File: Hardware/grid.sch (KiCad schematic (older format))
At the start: 269 parts, among them Q1 BSS83P, Q10 BSS83P, Q11 BSS83P, Q12 BSS83P, Q13 BSS83P, Q14 BSS83P, Q15 BSS83P, Q16 BSS83P, Q17 BSS83P, Q18 BSS83P, Q19 BSS83P, Q2 BSS83P, Q20 BSS83P, Q21 NX7002AK, Q22 NX7002AK, Q23 NX7002AK, Q24 NX7002AK, Q25 NX7002AK, Q26 NX7002AK, Q27 NX7002AK, Q28 NX7002AK, Q29 NX7002AK, Q3 BSS83P, Q30 NX7002AK, Q31 NX7002AK, Q32 NX7002AK, Q4 BSS83P, Q5 BSS83P, Q6 BSS83P, Q7 BSS83P, Q8 BSS83P, Q9 BSS83P, SW1 Button_matrix_4x4, SW10 SW_Push, SW11 SW_Push, SW12 SW_Push, SW13 SW_Push, SW14 SW_Push, SW15 SW_Push, SW16 SW_Push, SW17 SW_Push, SW18 SW_Push, SW19 SW_Push, SW2 Button_matrix_4x4, SW20 SW_Push, SW3 Button_matrix_4x4, SW4 Button_matrix_4x4, SW5 SW_Push, SW6 SW_Push, SW7 SW_Push, SW8 SW_Push, SW9 SW_Push, U2 74HC138, U3 74HC138, U4 74HC138

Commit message: linked footprints with 3D models in project directory
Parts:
- R21, R22, R23, R24: value 10K -> 1K
- R25, R26, R27, R28, R33, R34, R35, R36, R41, R42, R43, R44: value 100 -> 100R
- U2, U3, U4: Catalog link (none) -> http://uk.farnell.com/texas-instruments/sn74hc138pw/ic-deco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
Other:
- moved on the sheet: Q21, Q22, Q23, Q24, Q25, Q26, Q27, Q28, Q29, Q30, Q31, Q32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

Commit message: added BOM, changed names of some components in the schematic
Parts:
- Q1, Q10, Q11, Q12, Q13, Q14, Q15, Q16, Q17, Q18, Q19, Q2, Q20, Q3, Q4, Q5, Q6, Q7, Q8, Q9: value BSS83P -> BSH205G2
- U2, U3, U4: value 74HC138 -> SN74HC138PW
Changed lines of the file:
@@
 P 8200 2750
 F 0 "Q2" H 7900 2900 50  0000 L CNN
-F 1 "BSS83P" H 7900 3000 50  0000 L CNN
+F 1 "BSH205G2" H 7900 3000 50  0000 L CNN
 F 2 "project_library:SOT-23" H 8400 2675 50  0001 L CIN
 F 3 "" H 8200 2750 50  0001 L CNN
@@
 P 7650 2750
 F 0 "Q1" H 7350 2900 50  0000 L CNN
-F 1 "BSS83P" H 7350 3000 50  0000 L CNN
+F 1 "BSH205G2" H 7350 3000 50  0000 L CNN
 F 2 "project_library:SOT-23" H 7850 2675 50  0001 L CIN
 F 3 "" H 7650 2750 50  0001 L CNN
@@
 P 9450 2750
 F 0 "Q4" H 9150 2900 50  0000 L CNN
-F 1 "BSS83P" H 9150 3000 50  0000 L CNN
+F 1 "BSH205G2" H 9150 3000 50  0000 L CNN
 F 2 "project_library:SOT-23" H 9650 2675 50  0001 L CIN
 F 3 "" H 9450 2750 50  0001 L CNN
@@
 P 8900 2750
 F 0 "Q3" H 8600 2900 50  0000 L CNN
-F 1 "BSS83P" H 8600 3000 50  0000 L CNN
+F 1 "BSH205G2" H 8600 3000 50  0000 L CNN
 F 2 "project_library:SOT-23" H 9100 2675 50  0001 L CIN
 F 3 "" H 8900 2750 50  0001 L CNN
@@
 P 10700 2750
 F 0 "Q6" H 10400 2900 50  0000 L CNN
-F 1 "BSS83P" H 10400 3000 50  0000 L CNN
+F 1 "BSH205G2" H 10400 3000 50  0000 L CNN
 F 2 "project_library:SOT-23" H 10900 2675 50  0001 L CIN
 F 3 "" H 10700 2750 50  0001 L CNN
@@
 P 10150 2750
 F 0 "Q5" H 9850 2900 50  0000 L CNN
-F 1 "BSS83P" H 9850 3000 50  0000 L CNN
+F 1 "BSH205G2" H 9850 3000 50  0000 L CNN
 F 2 "project_library:SOT-23" H 10350 2675 50  0001 L CIN
 F 3 "" H 10150 2750 50  0001 L CNN
@@
 P 11950 2750
 F 0 "Q8" H 11650 2900 50  0000 L CNN
-F 1 "BSS83P" H 11650 3000 50  0000 L CNN
+F 1 "BSH205G2" H 11650 3000 50  0000 L CNN
 F 2 "project_library:SOT-23" H 12150 2675 50  0001 L CIN
 F 3 "" H 11950 2750 50  0001 L CNN
@@
 P 11400 2750
 F 0 "Q7" H 11100 2900 50  0000 L CNN
-F 1 "BSS83P" H 11100 3000 50  0000 L CNN
+F 1 "BSH205G2" H 11100 3000 50  0000 L CNN
 F 2 "project_library:SOT-23" H 11600 2675 50  0001 L CIN
 F 3 "" H 11400 2750 50  0001 L CNN
@@
 P 13200 2750
 F 0 "Q10" H 12900 2900 50  0000 L CNN
-F 1 "BSS83P" H 12900 3000 50  0000 L CNN
+F 1 "BSH205G2" H 12900 3000 50  0000 L CNN
 F 2 "project_library:SOT-23" H 13400 2675 50  0001 L CIN
 F 3 "" H 13200 2750 50  0001 L CNN
@@
 P 12650 2750
 F 0 "Q9" H 12350 2900 50  0000 L CNN
-F 1 "BSS83P" H 12350 3000 50  0000 L CNN
+F 1 "BSH205G2" H 12350 3000 50  0000 L CNN
 F 2 "project_library:SOT-23" H 12850 2675 50  0001 L CIN
 F 3 "" H 12650 2750 50  0001 L CNN
@@
 P 14450 2750
 F 0 "Q12" H 14150 2900 50  0000 L CNN
-F 1 "BSS83P" H 14150 3000 50  0000 L CNN
+F 1 "BSH205G2" H 14150 3000 50  0000 L CNN
 F 2 "project_library:SOT-23" H 14650 2675 50  0001 L CIN
 F 3 "" H 14450 2750 50  0001 L CNN
@@
 P 13900 2750
 F 0 "Q11" H 13600 2900 50  0000 L CNN
-F 1 "BSS83P" H 13600 3000 50  0000 L CNN
+F 1 "BSH205G2" H 13600 3000 50  0000 L CNN
 F 2 "project_library:SOT-23" H 14100 2675 50  0001 L CIN
 F 3 "" H 13900 2750 50  0001 L CNN
@@
 P 15700 2750
 F 0 "Q14" H 15400 2900 50  0000 L CNN
-F 1 "BSS83P" H 15400 3000 50  0000 L CNN
+F 1 "BSH205G2" H 15400 3000 50  0000 L CNN
 F 2 "project_library:SOT-23" H 15900 2675 50  0001 L CIN
 F 3 "" H 15700 2750 50  0001 L CNN
@@
 P 15150 2750
 F 0 "Q13" H 14850 2900 50  0000 L CNN
-F 1 "BSS83P" H 14850 3000 50  0000 L CNN
+F 1 "BSH205G2" H 14850 3000 50  0000 L CNN
 F 2 "project_library:SOT-23" H 15350 2675 50  0001 L CIN
 F 3 "" H 15150 2750 50  0001 L CNN
@@
 P 16950 2750
 F 0 "Q16" H 16650 2900 50  0000 L CNN
-F 1 "BSS83P" H 16650 3000 50  0000 L CNN
+F 1 "BSH205G2" H 16650 3000 50  0000 L CNN
 F 2 "project_library:SOT-23" H 17150 2675 50  0001 L CIN
 F 3 "" H 16950 2750 50  0001 L CNN
@@
 P 16400 2750
 F 0 "Q15" H 16100 2900 50  0000 L CNN
-F 1 "BSS83P" H 16100 3000 50  0000 L CNN
+F 1 "BSH205G2" H 16100 3000 50  0000 L CNN
 F 2 "project_library:SOT-23" H 16600 2675 50  0001 L CIN
 F 3 "" H 16400 2750 50  0001 L CNN
@@
 P 10250 13500
 F 0 "U4" H 10350 14000 50  0000 C CNN
-F 1 "74HC138" H 10550 13000 50  0000 C CNN
+F 1 "SN74HC138PW" H 10550 13000 50  0000 C CNN
 F 2 "project_library:TSSOP-16_4.4x5mm_Pitch0.65mm" H 10250 13500 50  0001 C CNN
 F 3 "" H 10250 13500 50  0001 C CNN
@@
 P 7700 13500
 F 0 "U3" H 7800 14000 50  0000 C CNN
-F 1 "74HC138" H 8000 13000 50  0000 C CNN
+F 1 "SN74HC138PW" H 8000 13000 50  0000 C CNN
 F 2 "project_library:TSSOP-16_4.4x5mm_Pitch0.65mm" H 7700 13500 50  0001 C CNN
 F 3 "" H 7700 13500 50  0001 C CNN
@@
 P 5150 13500
 F 0 "U2" H 5250 14000 50  0000 C CNN
-F 1 "74HC138" H 5450 13000 50  0000 C CNN
+F 1 "SN74HC138PW" H 5450 13000 50  0000 C CNN
 F 2 "project_library:TSSOP-16_4.4x5mm_Pitch0.65mm" H 5150 13500 50  0001 C CNN
 F 3 "" H 5150 13500 50  0001 C CNN
@@
 P 18700 2750
 F 0 "Q18" H 18400 2900 50  0000 L CNN
-F 1 "BSS83P" H 18400 3000 50  0000 L CNN
+F 1 "BSH205G2" H 18400 3000 50  0000 L CNN
 F 2 "project_library:SOT-23" H 18900 2675 50  0001 L CIN
 F 3 "" H 18700 2750 50  0001 L CNN
@@
 P 18150 2750
 F 0 "Q17" H 17850 2900 50  0000 L CNN
-F 1 "BSS83P" H 17850 3000 50  0000 L CNN
+F 1 "BSH205G2" H 17850 3000 50  0000 L CNN
 F 2 "project_library:SOT-23" H 18350 2675 50  0001 L CIN
 F 3 "" H 18150 2750 50  0001 L CNN
@@
 P 19950 2750
 F 0 "Q20" H 19650 2900 50  0000 L CNN
-F 1 "BSS83P" H 19650 3000 50  0000 L CNN
+F 1 "BSH205G2" H 19650 3000 50  0000 L CNN
 F 2 "project_library:SOT-23" H 20150 2675 50  0001 L CIN
 F 3 "" H 19950 2750 50  0001 L CNN
@@
 P 19400 2750
 F 0 "Q19" H 19100 2900 50  0000 L CNN
-F 1 "BSS83P" H 19100 3000 50  0000 L CNN
+F 1 "BSH205G2" H 19100 3000 50  0000 L CNN
 F 2 "project_library:SOT-23" H 19600 2675 50  0001 L CIN
 F 3 "" H 19400 2750 50  0001 L CNN

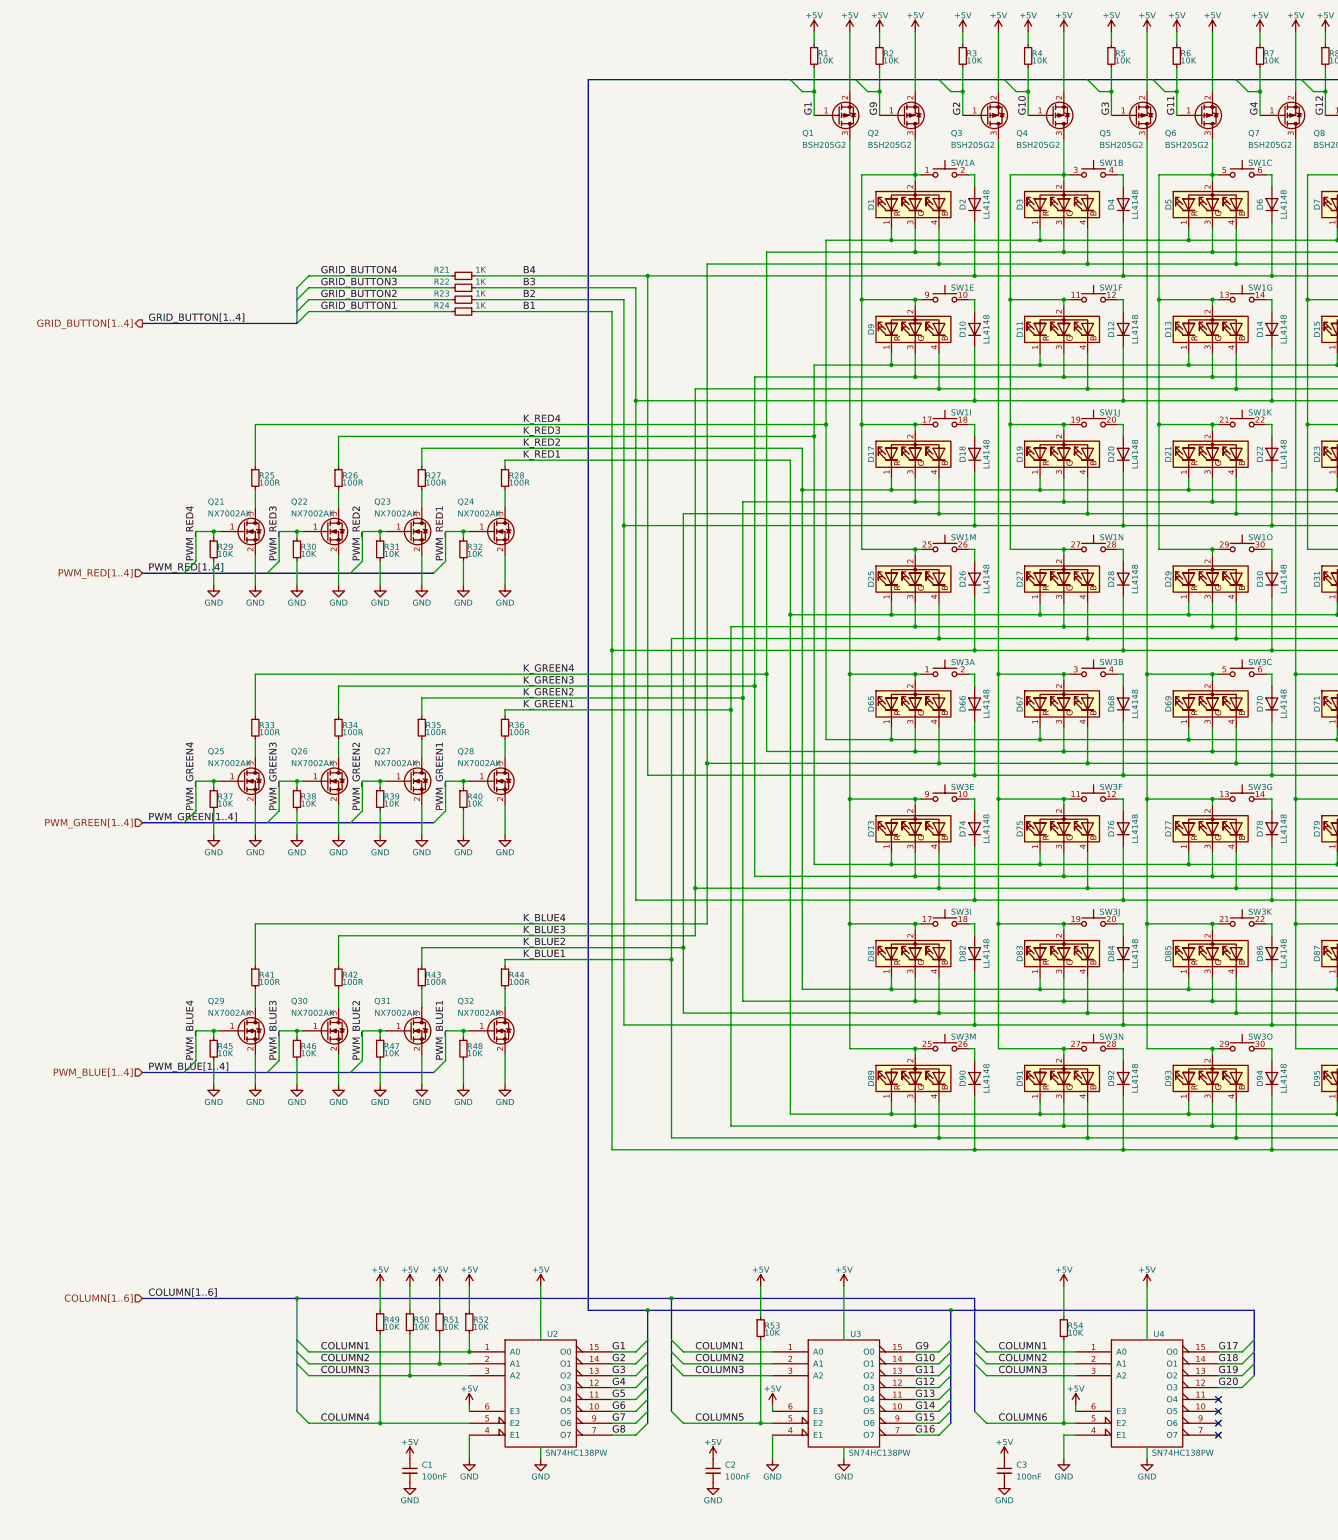
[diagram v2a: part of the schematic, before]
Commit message: copied project cache library to project_library.lib
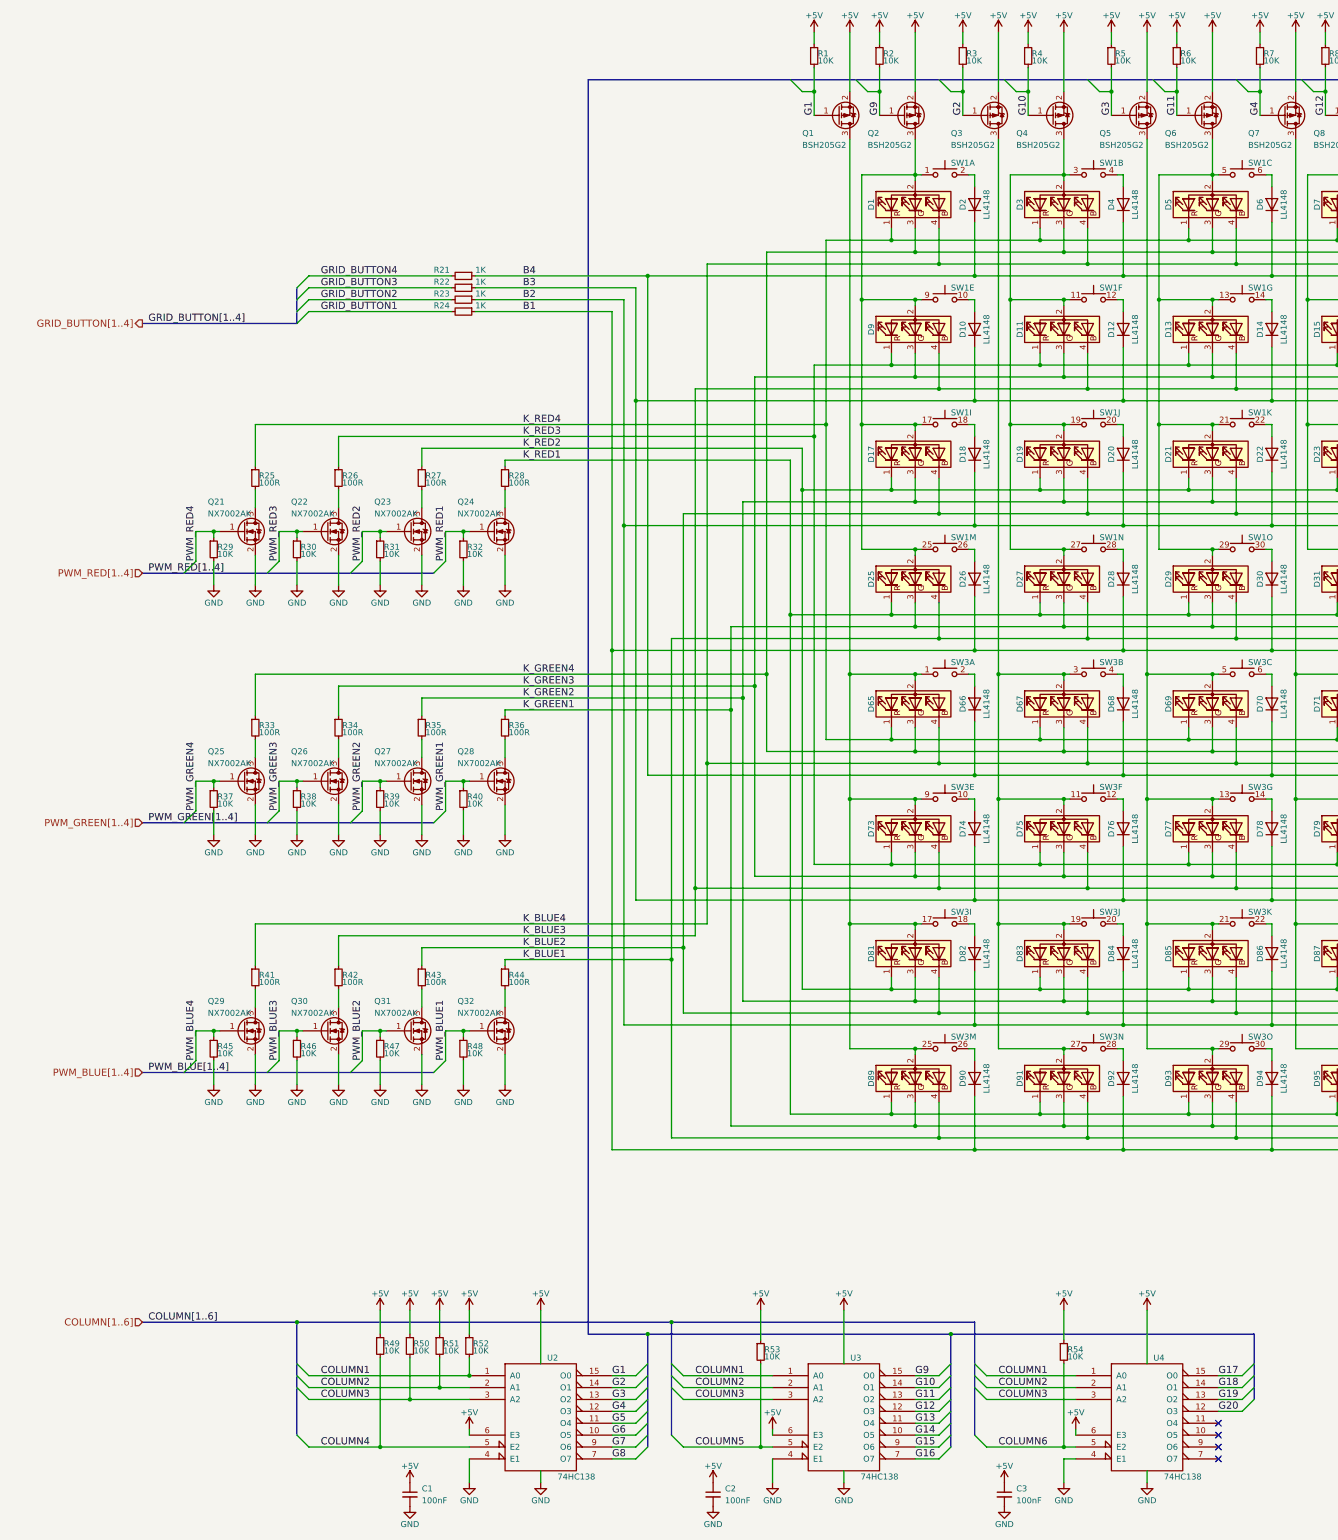
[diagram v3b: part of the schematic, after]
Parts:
- U2, U3, U4: value SN74HC138PW -> 74HC138
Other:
- moved on the sheet: C1, C2, C3, R49, R50, R51, R52, R53, R54, U2, U3, U4
